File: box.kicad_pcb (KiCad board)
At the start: 2 copper layers, 140 x 140.2 mm, 151 parts, among them J101 Connector_Generic:Conn_02x20_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, J102 Connector_Generic:Conn_02x20_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, J103 Conn_01x05, J104 Conn_01x05, J801 Conn_01x03, J901 Conn_01x03, K201 Conn_01x04, K202 Conn_01x04, K203 Conn_01x04, K204 Conn_01x04, K301 Conn_01x04, K302 Conn_01x04, K303 Conn_01x04, K304 Conn_01x04, K401 Conn_01x04, K402 Conn_01x04, K403 Conn_01x04, K404 Conn_01x04, K501 Conn_01x04, K502 Conn_01x04, K503 Conn_01x04, K504 Conn_01x04, K601 Conn_01x04, K602 Conn_01x04, K603 Conn_01x04, K604 Conn_01x04, K701 Conn_01x04, K702 Conn_01x04, K703 Conn_01x04, K704 Conn_01x04, P101 Conn_01x03_Male, P102 Conn_01x03_Male, P103 Conn_01x03_Male, P104 Conn_01x03_Male, P105 Conn_01x03_Male, P106 Conn_01x03_Male, P107 Conn_01x03_Male, P108 Conn_01x03_Male, U101 Connector_Generic:Conn_02x20_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

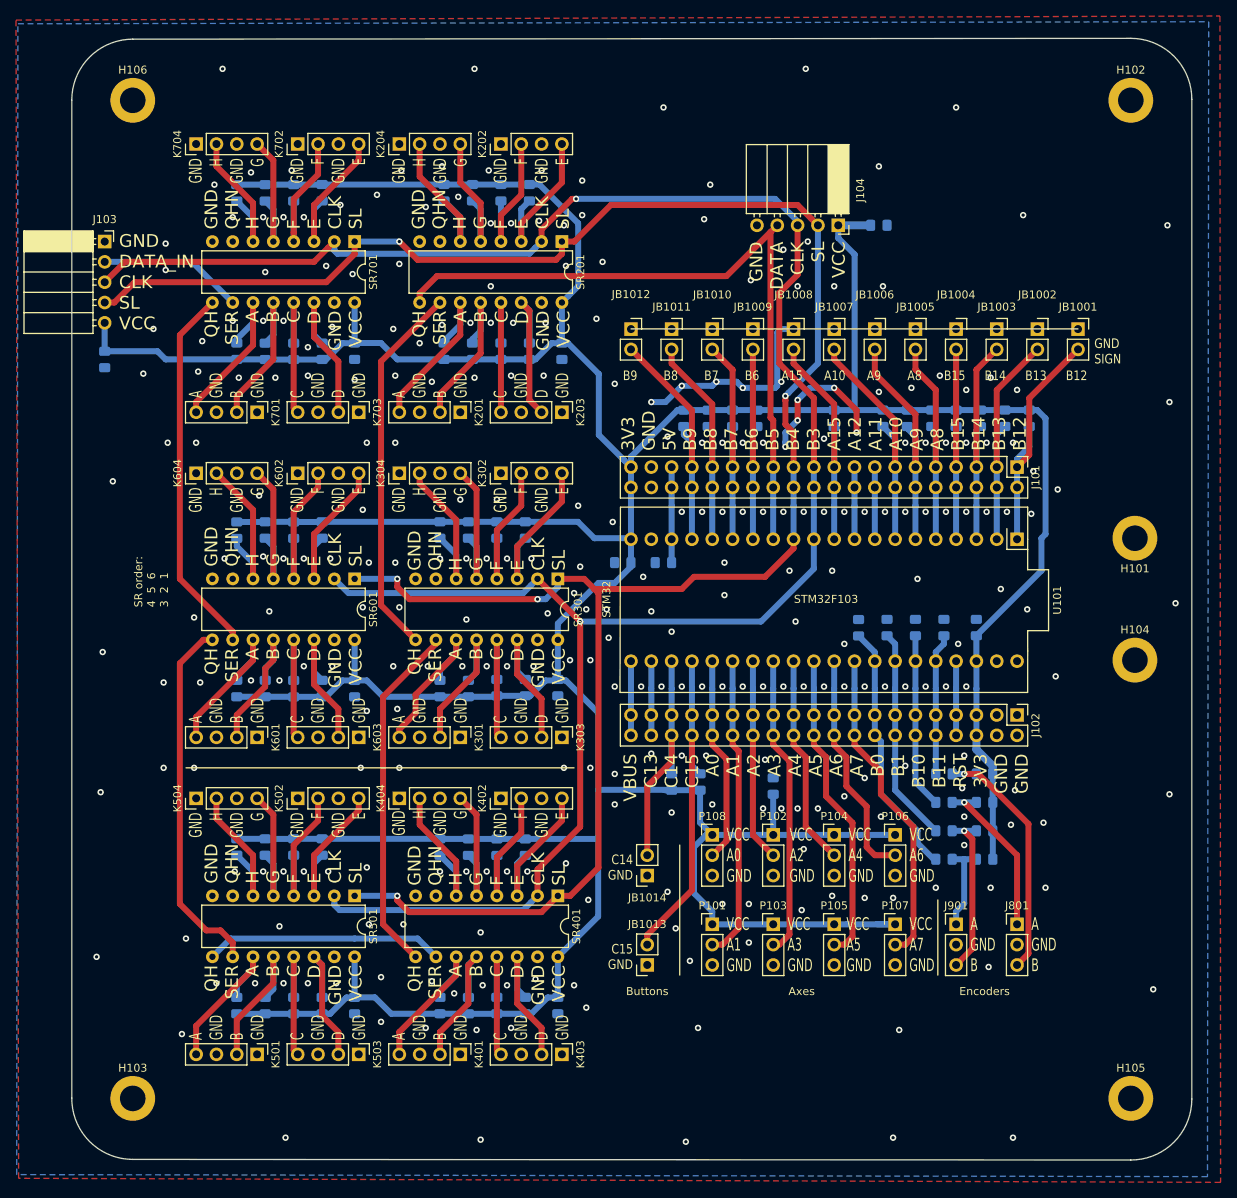
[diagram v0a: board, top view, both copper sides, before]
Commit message: New layout
Moved connectors to edges, shrunk board size from 14x14 cm to 14x9 cm.
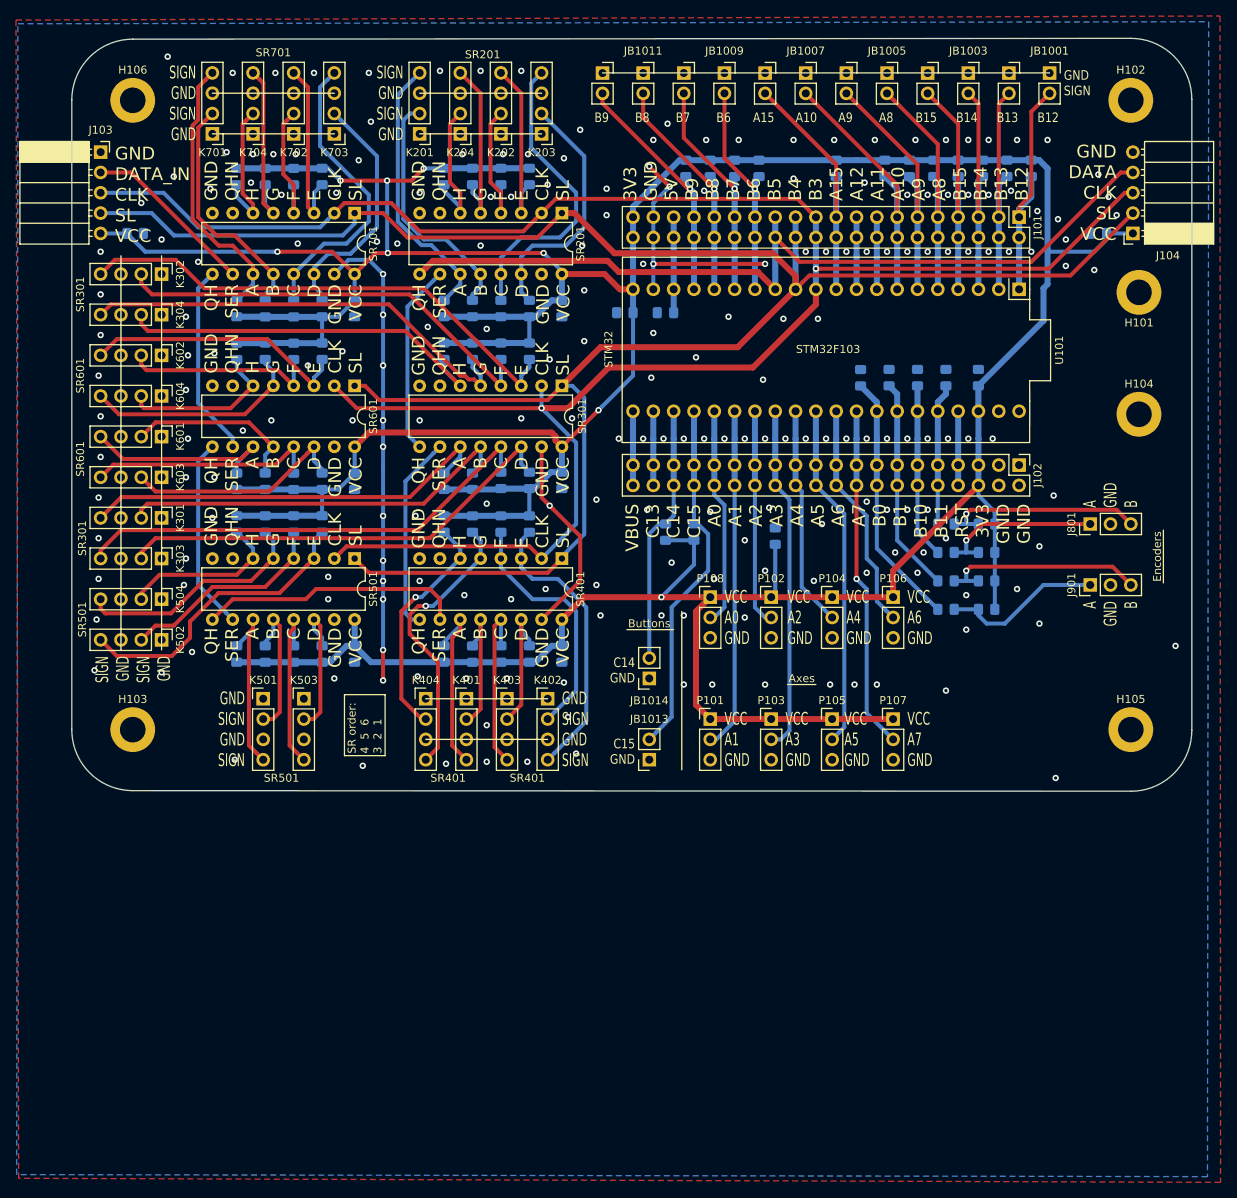
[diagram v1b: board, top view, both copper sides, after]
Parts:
- moved K303 54.8 mm to (38.9, 94.0)
- moved J801 50.9 mm to (154.9, 89.7), turned to 90 degrees
- moved K302 49.2 mm to (38.9, 58.4), turned to 270 degrees
- moved K301 46.3 mm to (38.9, 88.9)
- moved H103 46.1 mm to (35.3, 115.4)
- moved H105 46.1 mm to (160.0, 115.4)
- moved J901 45.6 mm to (154.9, 97.3), turned to 90 degrees
- moved K403 45.0 mm to (82.0, 111.5), turned to 0 degrees
- moved K503 45.0 mm to (56.6, 111.5), turned to 0 degrees
- moved K401 44.5 mm to (77.0, 111.5), turned to 0 degrees
- moved K501 44.5 mm to (51.6, 111.5), turned to 0 degrees
- moved C401 43.9 mm to (88.9, 105.9)
- moved R401 43.9 mm to (74.2, 105.9)
- moved R403 43.9 mm to (77.7, 105.9)
- moved R405 43.9 mm to (81.3, 105.9)
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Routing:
- net GND: track 44.5 -> 115.2 mm, vias 297 -> 219
- net /Shift register 2/E: track 21.0 -> 63.6 mm
- net /Shift register 2/C: track 17.4 -> 59.6 mm
- net /Shift register 2/D: track 18.8 -> 57.3 mm
- net /Shift register 2/G: track 19.6 -> 56.0 mm
- net +3V3: track 646.1 -> 610.3 mm, vias 0 -> 8
- net /Shift register 2/F: track 19.6 -> 54.8 mm
- net /Shift register 2/A: track 21.0 -> 52.8 mm
- net /Shift register 2/B: track 19.6 -> 50.4 mm
- net /Shift register 2/H: track 21.0 -> 48.4 mm
- net /SR_DATA_2: track 47.0 -> 23.9 mm
- net /SR_DATA_6: track 46.6 -> 24.1 mm
- net /SR_DATA_5: track 45.7 -> 24.1 mm
- net /SR_DATA_3: track 44.0 -> 24.7 mm
- net /Shift register/C: track 18.8 -> 38.0 mm
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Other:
- board size 140 x 140.2 mm -> 140 x 94.1 mm
- board text added: "GND SIGN GND SIGN"
- board text added: "SIGN GND SIGN GND"
- board text added: "SR201"
- board text added: "SR301"
- board text added: "SR401"
- board text added: "SR501"
- board text added: "SR601"
- board text added: "SR701"
- board text removed: "A GND B GND"
- board text removed: "C GND D GND"
- board text removed: "GND F GND E"
- board text removed: "GND H GND G"

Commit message: First version released
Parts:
- moved H103 0.11 mm to (35.3, 115.3)
- moved H105 0.11 mm to (160.0, 115.3)
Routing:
- net /Shift register/B: track 31.0 -> 31.8 mm
- net /Shift register 2/A: track 52.8 -> 53.5 mm
- net /Shift register 2/D: track 57.3 -> 57.9 mm
- net GND: vias 219 -> 241
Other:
- board size 140 x 94.1 mm -> 140 x 94 mm
- board text added: "2020-05-28 STM32 button box v1 aapalo"
- board text added: "GND DATA_OUT CLK SL VCC"
- board text added: "SR_CLK"
- board text added: "SR_DATA"
- board text added: "SR_LS"
- board text removed: "2020-05-25 STM32 button box v1 aapalo"
